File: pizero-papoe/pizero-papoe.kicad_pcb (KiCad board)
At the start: 2 copper layers, 81.8 x 30 mm, 67 parts, among them J1 RJ45-LED, P2 dnp-REF-182665-01, Q2 DMMT3906_Dual_PNP, Q3 Q_PMOS_GSD, T1 H2019FNL, U1 ENC28J60-I/ML, U2 TPS63070RNMR, U3 nostuff-AT24CS32-SSHM, U4 AP7365_SOT-23-5, Y1 25Mhz

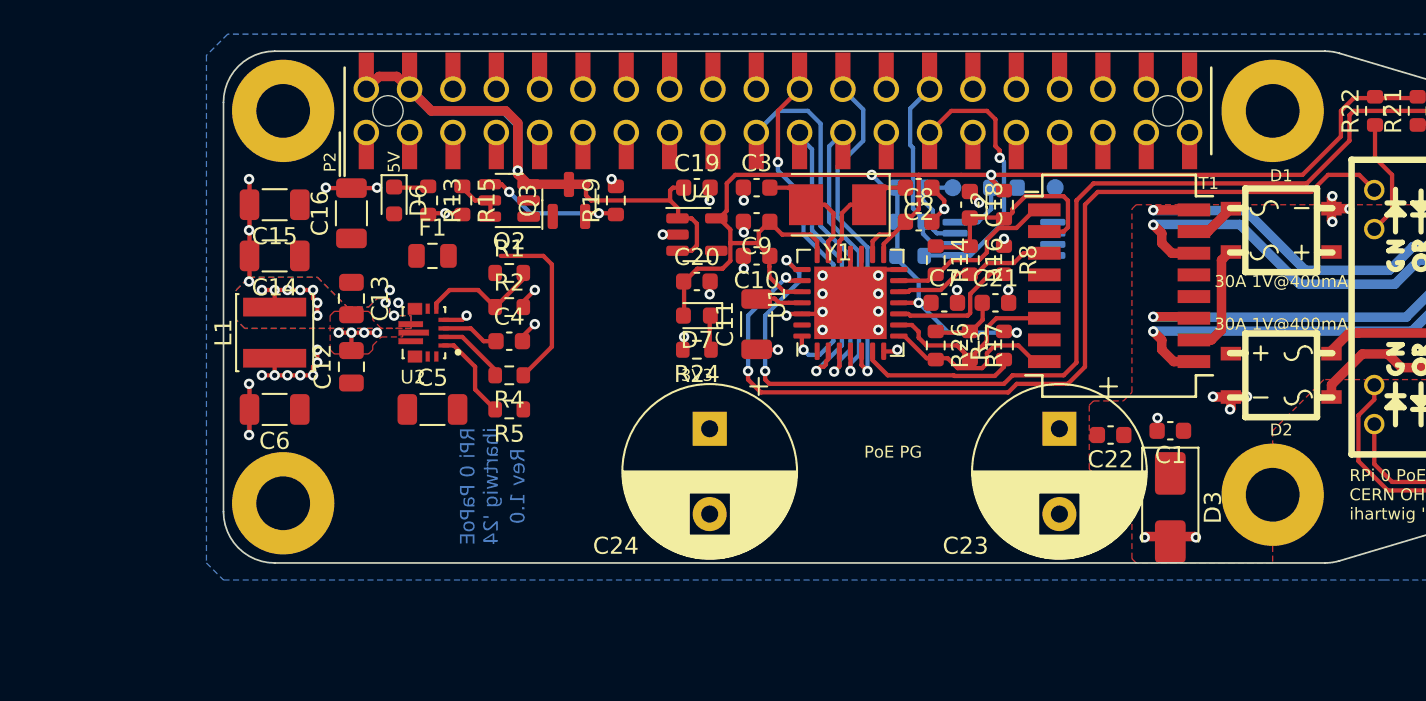
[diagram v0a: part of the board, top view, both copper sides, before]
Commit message: sch updates for RTL8153B and RJE7318800240
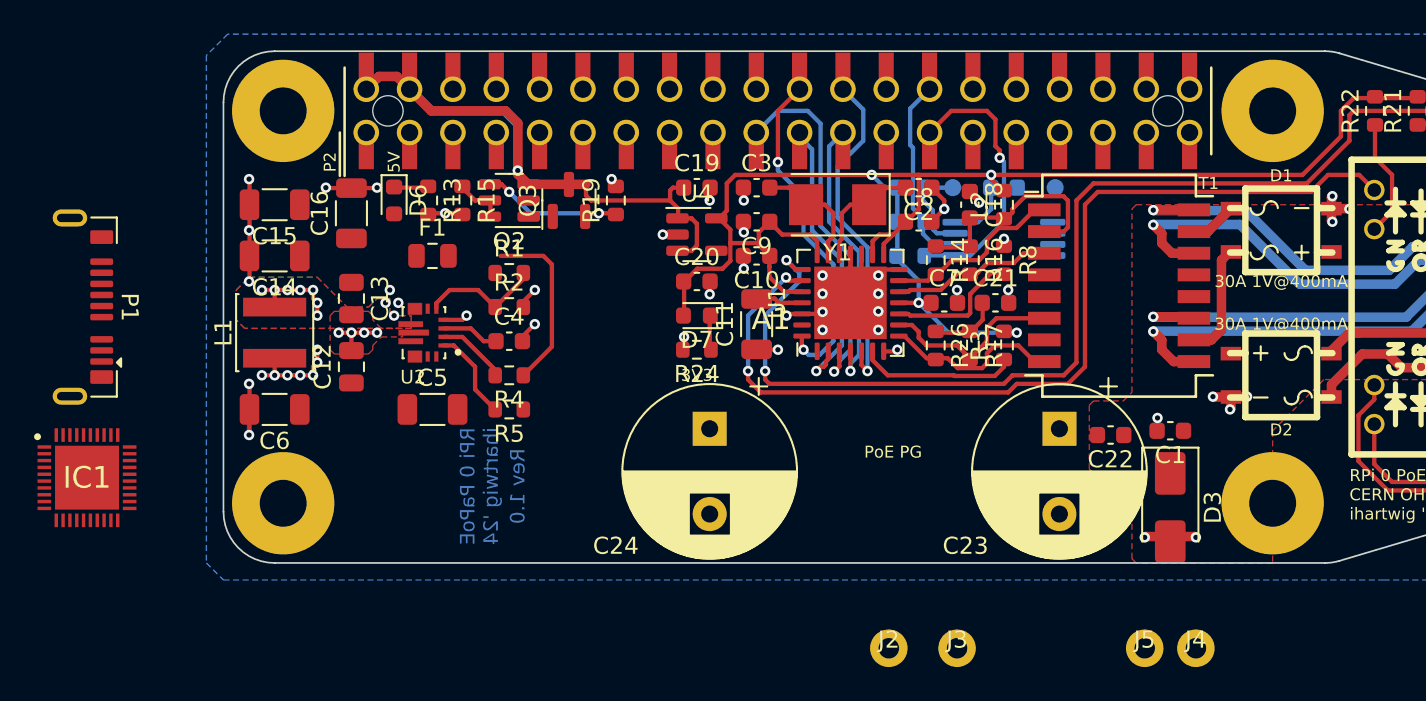
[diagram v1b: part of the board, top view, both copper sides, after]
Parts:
- removed H1, H2, H3, H4: hole-metalized-no4, pizero-poe-special:hole-m3
- added A1: Raspberry Pi Zero/W/2W, Raspberry_Pi_Zero_v.1.3_Hat:RPi_Zero_ZeroW_Zero2W_Hat_NoPads_NoHeader, F.Cu at (171.1, 107.7)
- added IC1: RTL8153B-VB-CG, pizero-poe-special:RTL8153B-VB-CG_QFN40P500X500X90-41N-D, F.Cu at (98.1, 102.7)
- added J2: PogoPin_01x01, pizero-poe-special:PogoPin_CPG-04-TH-TR, F.Cu at (145.1, 112.7)
- added J3: PogoPin_01x01, pizero-poe-special:PogoPin_CPG-04-TH-TR, F.Cu at (149.1, 112.7)
- added J4: PogoPin_01x01, pizero-poe-special:PogoPin_CPG-04-TH-TR, F.Cu at (163.1, 112.7)
- added J5: PogoPin_01x01, pizero-poe-special:PogoPin_CPG-04-TH-TR, F.Cu at (160.1, 112.7)
- added P1: USB_C_Plug_USB3.0_9P, pizero-poe-special:USB_C_Plug_G-Switch_GT-USB-8016A_9P_TopMnt_Horizontal, F.Cu at (97.1, 92.7)

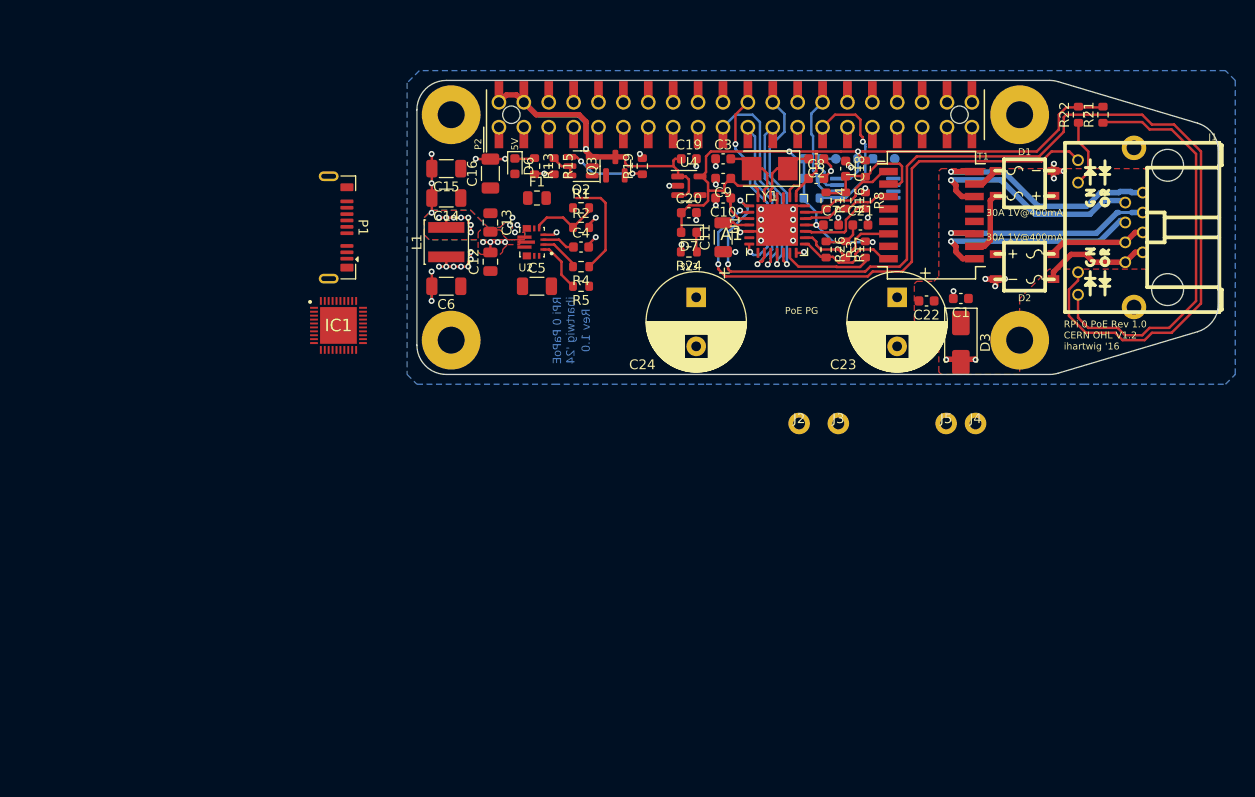
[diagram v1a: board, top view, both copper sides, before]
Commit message: complete RTL8153B sch
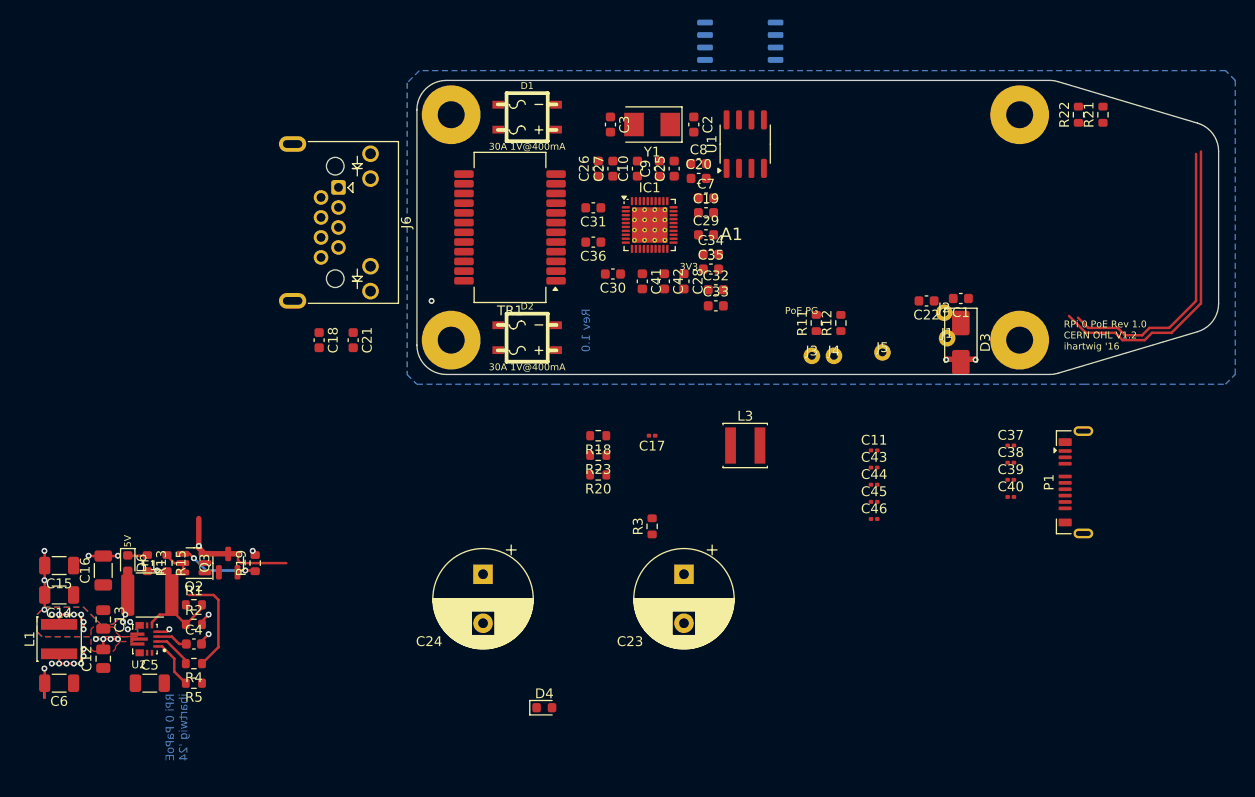
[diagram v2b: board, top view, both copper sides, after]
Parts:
- removed D7: LED Green, LED_SMD:LED_0603_1608Metric
- removed L2: BEAD, Resistor_SMD:R_0603_1608Metric
- removed P2: dnp-REF-182665-01, pizero-poe-special:Pin_Header_Straight_TH-SMT-NoPaste_2x20
- removed R14, R16, R17, R26: 49.9, Resistor_SMD:R_0603_1608Metric
- removed R24: 220, Resistor_SMD:R_0603_1608Metric
- removed R8: 2.32k, Resistor_SMD:R_0603_1608Metric
- removed T1: H2019FNL, pizero-poe-special:Transformer_Pulse_H2019FNL
- removed U4: AP7365_SOT-23-5, Package_TO_SOT_SMD:SOT-23-5
- removed W1, W2: TEST_1P, TestPoint:TestPoint_Pad_D1.0mm
- added C25: 0.1uf, Capacitor_SMD:C_0603_1608Metric, F.Cu at (132.3, 86.7)
- added C26: 0.1uf, Capacitor_SMD:C_0603_1608Metric, F.Cu at (124.6, 86.7)
- added C27: 0.1uf, Capacitor_SMD:C_0603_1608Metric, F.Cu at (126.1, 86.7)
- added C28: 0.1uf, Capacitor_SMD:C_0603_1608Metric, F.Cu at (133.3, 98.2)
- added C29: 0.1uf, Capacitor_SMD:C_0603_1608Metric, F.Cu at (135.6, 93.5)
- added C30: 0.1uf, Capacitor_SMD:C_0603_1608Metric, F.Cu at (126.1, 97.5)
- added C31: 0.1uf, Capacitor_SMD:C_0603_1608Metric, F.Cu at (124.1, 90.7)
- added C32: 4.7uF, Capacitor_SMD:C_0603_1608Metric, F.Cu at (136.6, 99.1)
- added C33: 0.1uf, Capacitor_SMD:C_0603_1608Metric, F.Cu at (136.6, 100.7)
- added C34: 1uF, Capacitor_SMD:C_0603_1608Metric, F.Cu at (136.1, 95.5)
- added C35: 0.1uf, Capacitor_SMD:C_0603_1608Metric, F.Cu at (136.1, 97.0)
- added C36: 0.1uf, Capacitor_SMD:C_0603_1608Metric, F.Cu at (124.1, 94.2)
- added C37: 0.1uF 0201, Capacitor_SMD:C_0201_0603Metric, F.Cu at (166.7, 115.0)
- added C38: 0.1uF 0201, Capacitor_SMD:C_0201_0603Metric, F.Cu at (166.7, 116.7)
- added C39: 0.1uF 0201, Capacitor_SMD:C_0201_0603Metric, F.Cu at (166.7, 118.5)
- added C40: 0.1uF 0201, Capacitor_SMD:C_0201_0603Metric, F.Cu at (166.7, 120.2)
- added C41: 0.1uf, Capacitor_SMD:C_0603_1608Metric, F.Cu at (129.1, 98.2)
- added C42: 0.1uf, Capacitor_SMD:C_0603_1608Metric, F.Cu at (131.3, 98.2)
- added C43: 0.1uF, Capacitor_SMD:C_0201_0603Metric, F.Cu at (152.8, 117.2)
- added C44: 0.1uF, Capacitor_SMD:C_0201_0603Metric, F.Cu at (152.8, 119.0)
- added C45: 0.1uF, Capacitor_SMD:C_0201_0603Metric, F.Cu at (152.8, 120.7)
- added C46: 0.1uF, Capacitor_SMD:C_0201_0603Metric, F.Cu at (152.8, 122.5)
- added D4: LED Orange, LED_SMD:LED_0603_1608Metric, F.Cu at (119.1, 141.7)
- added J6: RJ45_LED_AK_Shielded, pizero-poe-special:RJ45_Amphenol_RJE7318800xxx0x, F.Cu at (97.8, 92.2)
- added L3: 2.2uH, Inductor_SMD:L_Sunlord_SWPA4030S, F.Cu at (139.6, 115.0)
- added R11: 22, Resistor_SMD:R_0603_1608Metric, F.Cu at (146.8, 102.5)
- added R12: 22, Resistor_SMD:R_0603_1608Metric, F.Cu at (149.4, 102.5)
- added TR1: 30F-51NL, Transformer_SMD:Transformer_Ethernet_YDS_30F-51NL_SO-24_7.1x15.1mm, F.Cu at (115.6, 92.7)
- C11: value 10uf -> 0.1uF; footprint Capacitor_SMD:C_1206_3216Metric -> Capacitor_SMD:C_0201_0603Metric
- C17: value nostuff-0.1u -> 0.1uF; footprint Capacitor_SMD:C_0603_1608Metric -> Capacitor_SMD:C_0201_0603Metric; moved to F.Cu
- C18, C21: value 0.1uf -> 1nF
- C19, C20: value 1uF -> 4.7uF
- C2, C3: value 16pf -> 30pf
- F1: footprint Fuse:Fuse_0805_2012Metric -> pizero-poe-special:Fuse_2016_5041Metric
- IC1: footprint pizero-poe-special:RTL8153B-VB-CG_QFN40P500X500X90-41N-D -> Package_DFN_QFN:QFN-40-1EP_5x5mm_P0.4mm_EP3.6x3.6mm_ThermalVias
- J1: value RJ45-LED -> PogoPin_01x01; footprint pizero-poe-special:rj45-tyco-2-406549-7 -> pizero-poe-special:PogoPin_CPG-01-TH-TR
- J2, J3, J4, J5: footprint pizero-poe-special:PogoPin_CPG-04-TH-TR -> pizero-poe-special:PogoPin_CPG-01-TH-TR
- R18: value nostuff-1k -> 22-dnp; moved to F.Cu
- R20: value nostuff-3.9k -> 22-dnp; moved to F.Cu
- R21, R22: value 549 -> 1k
- R23: value nostuff-3.9k -> 10k; moved to F.Cu
- U1: value ENC28J60-I/ML -> 93LC46B; footprint Package_DFN_QFN:QFN-28-1EP_6x6mm_P0.65mm_EP4.25x4.25mm -> Package_SO:SOIC-8_3.9x4.9mm_P1.27mm
- U3: value nostuff-AT24CS32-SSHM -> MX25L3233FM1; footprint Package_SO:TSSOP-8_4.4x3mm_P0.65mm -> Package_SO:SOP-8_5.28x5.23mm_P1.27mm
- moved P1 81.3 mm to (174.1, 118.7), turned to 90 degrees
- moved C15 56.6 mm to (69.6, 127.2)
- moved C16 56.6 mm to (74.1, 127.7)
- moved D6 56.6 mm to (76.6, 127.0)
- moved Q2 56.6 mm to (83.3, 127.0)
- moved Q3 56.6 mm to (86.8, 127.0)
- moved R13 56.6 mm to (78.6, 127.0)
- moved R15 56.6 mm to (80.6, 127.0)
- moved R19 56.6 mm to (89.6, 127.0)
- moved C12 56.6 mm to (74.1, 136.7)
- moved C13 56.6 mm to (74.1, 132.7)
- moved C14 56.6 mm to (69.6, 130.2)
- moved C4 56.6 mm to (83.3, 135.2)
- moved C5 56.6 mm to (78.8, 139.2)
- moved C6 56.6 mm to (69.6, 139.2)
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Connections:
- C10 pad 1: +3V3 -> +1V0
- C11 pad 2: Net-(U1-VCAP) -> /TR1_CT
- C17 pad 1: +3V3 -> GND
- C17 pad 2: GND -> /TR1_CT
- C18 pad 1: GND -> /J1_SH_C
- C18 pad 2: Net-(T1-TDCT) -> GND
- C2 pad 2: /PHY_OSC1 -> /IC1_CKXTAL1
- C20 pad 1: +3V3 -> +1V0
- C21 pad 1: Net-(C21-Pad1) -> /J1_SH_C
- C3 pad 2: /PHY_OSC2 -> /IC1_CKXTAL2
- C7 pad 1: +3V3 -> /RPI_VBUS
- C8 pad 1: +3V3 -> +1V0
- C9 pad 1: +3V3 -> +1V0
- D1 pad 2: /DATA_PAIR_2 -> /J6_DB_C
- D1 pad 3: /DATA_PAIR_1 -> /J6_DA_C
- D2 pad 2: /SPARE_PAIR_2 -> /J6_DC_C
- D2 pad 3: /SPARE_PAIR_1 -> /J6_DD_C
- IC1 pad 1: unconnected-(IC1-MDIP0-Pad1) -> /IC1_MDIP0
- IC1 pad 10: unconnected-(IC1-MDIN3-Pad10) -> /IC1_MDIN3
- IC1 pad 11: unconnected-(IC1-AVDD33_1-Pad11) -> +3V3
- IC1 pad 12: unconnected-(IC1-U3SSTXN-Pad12) -> /IC1_U3SSTX_N
- IC1 pad 13: unconnected-(IC1-U3SSTXP-Pad13) -> /IC1_U3SSTX_P
- IC1 pad 14: unconnected-(IC1-U3VDD10-Pad14) -> +1V0
- IC1 pad 15: unconnected-(IC1-U3SSRXN-Pad15) -> /IC1_U3SSRX_N
- IC1 pad 16: unconnected-(IC1-U3SSRXP-Pad16) -> /IC1_U3SSRX_P
- IC1 pad 17: unconnected-(IC1-U2DM-Pad17) -> /IC1_U2DM
- IC1 pad 18: unconnected-(IC1-U2DP-Pad18) -> /IC1_U2DP
- IC1 pad 19: unconnected-(IC1-U2VDD10-Pad19) -> +1V0
- IC1 pad 2: unconnected-(IC1-MDIN0-Pad2) -> /IC1_MDIN0
- IC1 pad 20: unconnected-(IC1-AVDD33_2-Pad20) -> +3V3
- IC1 pad 21: unconnected-(IC1-VDD5-Pad21) -> /RPI_VBUS
- IC1 pad 22: unconnected-(IC1-DVDD10_UPS-Pad22) -> /IC1_DVDD10_UPS
- IC1 pad 23: unconnected-(IC1-DVDD33_1-Pad23) -> +3V3
- IC1 pad 24: unconnected-(IC1-EEDO/LED2/SPISDO/LANW/AKEB/GPIO-Pad24) -> /IC1_EED0_LED2
- IC1 pad 25: unconnected-(IC1-EEDI/SPISDI/ENSWREG-Pad25) -> /IC1_EEDI_ENSWREG
- IC1 pad 26: unconnected-(IC1-VDDREG33-Pad26) -> /RPI_VBUS
- IC1 pad 27: unconnected-(IC1-VDDREG5-Pad27) -> /RPI_VBUS
- IC1 pad 28: unconnected-(IC1-REGOUT-Pad28) -> /IC1_REGOUT
- IC1 pad 29: unconnected-(IC1-GND-Pad29) -> GND
- IC1 pad 3: unconnected-(IC1-AVDD10_1-Pad3) -> +1V0
- IC1 pad 30: unconnected-(IC1-EESK/LED1/SPISCK-Pad30) -> /IC1_LED1_SPISCK
- IC1 pad 31: unconnected-(IC1-EECS-Pad31) -> /IC1_EECS
- IC1 pad 32: unconnected-(IC1-LED0/SPICSB-Pad32) -> /IC1_LED0_SPICSB
- IC1 pad 33: unconnected-(IC1-DVDD33_2-Pad33) -> +3V3
- IC1 pad 34: unconnected-(IC1-DVDD10-Pad34) -> +1V0
- IC1 pad 35: unconnected-(IC1-CKXTAL1-Pad35) -> /IC1_CKXTAL1
- IC1 pad 36: unconnected-(IC1-CKXTAL2-Pad36) -> /IC1_CKXTAL2
- IC1 pad 37: unconnected-(IC1-AVDD10_3-Pad37) -> +1V0
- IC1 pad 39: unconnected-(IC1-AVDD33_3-Pad39) -> +3V3
- IC1 pad 4: unconnected-(IC1-MDIP1-Pad4) -> /IC1_MDIP1
- IC1 pad 40: unconnected-(IC1-AVDD33_4-Pad40) -> +3V3
- IC1 pad 41: unconnected-(IC1-EP-Pad41) -> GND
- IC1 pad 5: unconnected-(IC1-MDIN1-Pad5) -> /IC1_MDIN1
- IC1 pad 6: unconnected-(IC1-MDIP2-Pad6) -> /IC1_MDIP2
- IC1 pad 7: unconnected-(IC1-MDIN2-Pad7) -> /IC1_MDIN2
- IC1 pad 8: unconnected-(IC1-AVDD10_2-Pad8) -> +1V0
- IC1 pad 9: unconnected-(IC1-MDIP3-Pad9) -> /IC1_MDIP3
- J1 pad 1: /TPOUT_T+ -> GND
- J2 pad 1: unconnected-(J2-Pin_1-Pad1) -> /RPI_VBUS
- J3 pad 1: unconnected-(J3-Pin_1-Pad1) -> /J4_U2DM
- J4 pad 1: unconnected-(J4-Pin_1-Pad1) -> /J5_U2DP
- J5 pad 1: unconnected-(J5-Pin_1-Pad1) -> GND
- P1 pad A2: unconnected-(P1-TX1+-PadA2) -> /IC1_U3SSTX_C_P
- P1 pad A3: unconnected-(P1-TX1--PadA3) -> /IC1_U3SSTX_C_N
- P1 pad A6: unconnected-(P1-D+-PadA6) -> /P1_U2DP
- P1 pad A7: unconnected-(P1-D--PadA7) -> /P1_U2DM
- P1 pad B10: unconnected-(P1-RX1--PadB10) -> /IC1_U3SSRX_C_N
- P1 pad B11: unconnected-(P1-RX1+-PadB11) -> /IC1_U3SSRX_C_P
- R18 pad 1: +3V3 -> /P1_U2DM
- R18 pad 2: Net-(U3-WP) -> /IC1_U2DM
- R20 pad 1: +3V3 -> /P1_U2DP
- R20 pad 2: /GPIO0_ID_SD -> /IC1_U2DP
- R21 pad 1: /LEDB_A -> /J1_LED_YL_A
- R21 pad 2: +3V3 -> GND
- R22 pad 1: /LEDA_A -> /J1_LED_GN_A
- R22 pad 2: +3V3 -> GND
- R23 pad 2: /GPIO1_ID_SC -> /IC1_EEDI_ENSWREG
- R3 pad 1: Net-(U1-~{RESET}) -> Net-(D4-K)
- R3 pad 2: +3V3 -> GND
- U1 pad 1: unconnected-(U1-~{WOL}-Pad1) -> /IC1_EECS
- U1 pad 2: /GPIO9_MISO -> /IC1_LED1_SPISCK
- U1 pad 3: /GPIO10_MOSI -> /IC1_EEDI_ENSWREG
- U1 pad 4: /GPIO11_SCLK -> /IC1_EED0_LED2
- U1 pad 5: /GPIO8_CE0# -> GND
- U1 pad 6: Net-(U1-~{RESET}) -> unconnected-(U1-NC-Pad6)
- U1 pad 7: GND -> unconnected-(U1-NC-Pad7)
- U1 pad 8: /TPIN- -> +3V3
- U3 pad 1: GND -> /IC1_LED0_SPICSB
- U3 pad 2: GND -> /IC1_EED0_LED2
- U3 pad 3: GND -> +3V3
- U3 pad 5: /GPIO0_ID_SD -> /IC1_EEDI_ENSWREG
- U3 pad 6: /GPIO1_ID_SC -> /IC1_LED1_SPISCK
- U3 pad 7: Net-(U3-WP) -> +3V3
- Y1 pad 1: /PHY_OSC1 -> /IC1_CKXTAL1
- Y1 pad 2: /PHY_OSC2 -> /IC1_CKXTAL2
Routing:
- net /LEDB_K: track 108.6 -> 0.00 mm, vias 2 -> 0
- net +3V3: track 97.2 -> 0.00 mm, vias 4 -> 0
- net /LEDA_K: track 56.1 -> 0.00 mm, vias 2 -> 0
- net GND: track 77.9 -> 26.0 mm, vias 47 -> 18
- net /LEDB_A: track 42.4 -> 0.00 mm
- net (no net): track 91.1 -> 53.4 mm
- net /J1_LED_YL_A: track 0.00 -> 29.2 mm
- net /TPOUT_T+: track 24.1 -> 0.00 mm, vias 1 -> 0
- net /TPOUT_T-: track 23.3 -> 0.00 mm, vias 1 -> 0
- net /GPIO10_MOSI: track 22.9 -> 0.00 mm, vias 1 -> 0
- net /TPIN_T+: track 22.9 -> 0.00 mm, vias 1 -> 0
- net /TPIN_T-: track 22.2 -> 0.00 mm, vias 1 -> 0
- net /GPIO25: track 21.0 -> 0.00 mm, vias 2 -> 0
- net /GPIO8_CE0#: track 21.0 -> 0.00 mm, vias 1 -> 0
- net /GPIO9_MISO: track 18.5 -> 0.00 mm, vias 1 -> 0
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- removed copper zone on F.Cu, net /POE_VP

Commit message: pcb routing for RTL8153B and RJE7318800240
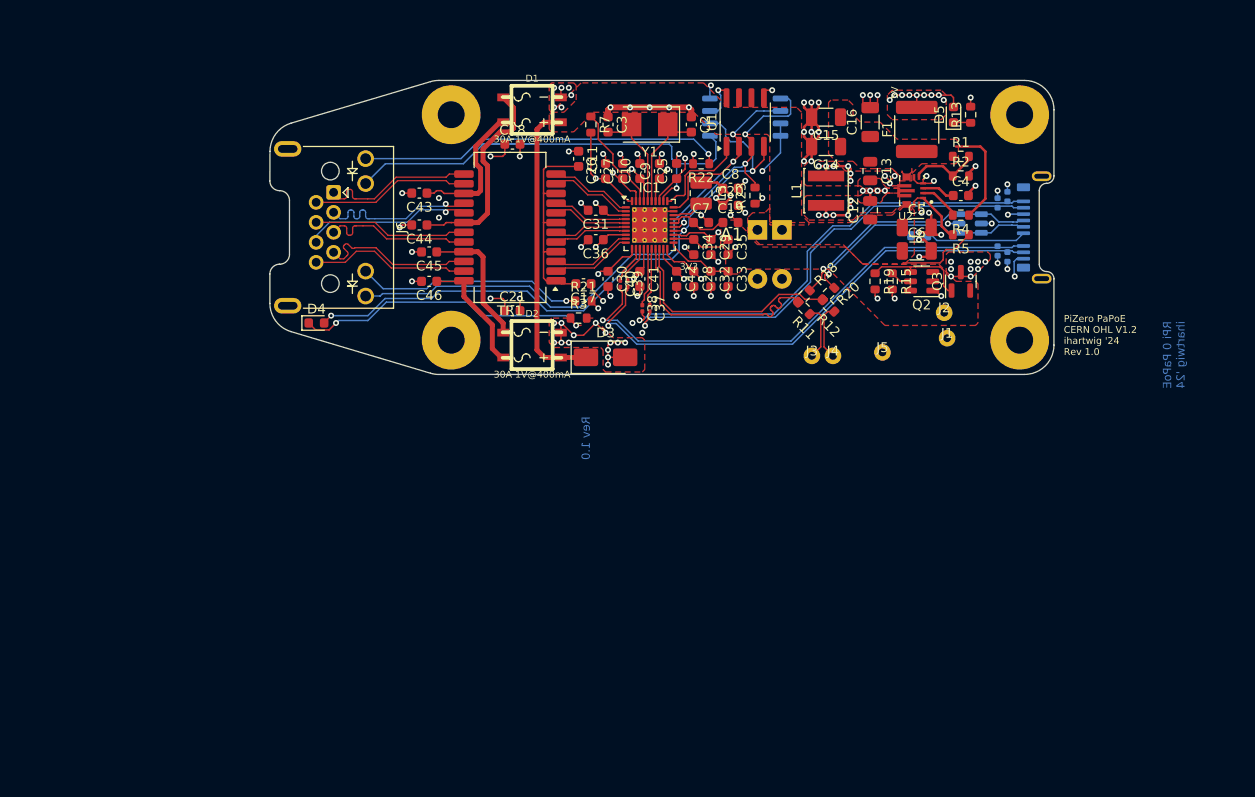
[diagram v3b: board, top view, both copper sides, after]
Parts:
- removed C1, C22: 0.1uf 100V, Capacitor_SMD:C_0603_1608Metric
- added D5: LED Green, LED_SMD:LED_0603_1608Metric, F.Cu at (160.8, 81.2)
- added D7: TPD1E01B04-dnp, Diode_SMD:D_0402_1005Metric, B.Cu at (165.3, 95.1)
- added D8: TPD1E01B04-dnp, Diode_SMD:D_0402_1005Metric, B.Cu at (165.3, 90.2)
- added D9: TPD1E01B04-dnp, Diode_SMD:D_0402_1005Metric, B.Cu at (166.3, 89.5)
- added R6: 5.1k, Resistor_SMD:R_0603_1608Metric, B.Cu at (157.3, 93.5)
- added R7: 10k, Resistor_SMD:R_0603_1608Metric, F.Cu at (123.8, 82.2)
- added U4: WE-TVS-82400102-dnp, Package_TO_SOT_SMD:SOT-23-6, B.Cu at (162.6, 92.3)
- C11, C17, C43, C44, C45, C46: footprint Capacitor_SMD:C_0201_0603Metric -> Capacitor_SMD:C_0603_1608Metric
- C23, C24, P1: moved to B.Cu
- D6: value LED Green -> TPD1E01B04-dnp; footprint LED_SMD:LED_0603_1608Metric -> Diode_SMD:D_0402_1005Metric; moved to B.Cu
- L3: footprint Inductor_SMD:L_Sunlord_SWPA4030S -> Inductor_SMD:L_1008_2520Metric
- moved C6 98.0 mm to (157.1, 95.1), turned to 0 degrees
- moved R13 95.7 mm to (162.6, 81.2), turned to 90 degrees
- moved D6 95.0 mm to (166.3, 95.7)
- moved F1 91.5 mm to (157.1, 82.7), turned to 90 degrees
- moved C5 91.0 mm to (157.1, 92.7)
- moved C12 90.6 mm to (152.3, 91.0)
- moved C13 90.6 mm to (152.3, 87.0)
- moved C14 90.6 mm to (147.8, 84.5)
- moved C15 90.6 mm to (147.8, 81.5)
- moved C16 90.6 mm to (152.3, 82.0)
- moved C4 90.6 mm to (161.6, 89.5)
- moved L1 90.6 mm to (147.8, 89.0)
- moved R1 90.6 mm to (161.6, 85.5)
- moved R2 90.6 mm to (161.6, 87.5)
- moved R4 90.6 mm to (161.6, 91.5)
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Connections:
- net /IC1_MDIN0 renamed /IC1_MDI0_N
- net /IC1_MDIN1 renamed /IC1_MDI1_N
- net /IC1_MDIN2 renamed /IC1_MDI2_N
- net /IC1_MDIN3 renamed /IC1_MDI3_N
- net /IC1_MDIP0 renamed /IC1_MDI0_P
- net /IC1_MDIP1 renamed /IC1_MDI1_P
- net /IC1_MDIP2 renamed /IC1_MDI2_P
- net /IC1_MDIP3 renamed /IC1_MDI3_P
- net /IC1_U2DM renamed /IC1_U2DN
- net /IC1_U3SSRX_C_N renamed /P1_U3SSRX_N
- net /IC1_U3SSRX_C_P renamed /P1_U3SSRX_P
- net /IC1_U3SSTX_C_N renamed /P1_U3SSTX_N
- net /J4_U2DM renamed /A1_U2DN
- net /J5_U2DP renamed /A1_U2DP
- net /J6_1_DA_P renamed /J6_DA_P
- net /J6_2_DA_N renamed /J6_DA_N
- net /J6_3_DB_P renamed /J6_DB_P
- net /J6_4_DC_P renamed /J6_DC_P
- net /J6_5_DC_N renamed /J6_DC_N
- net /J6_6_DB_N renamed /J6_DB_N
- net /J6_7_DD_P renamed /J6_DD_P
- net /J6_8_DD_N renamed /J6_DD_N
- net /P1_U2DM renamed /P1_U2DN
- C39 pad 2: /IC1_U3SSTX_C_P -> /P1_U3SSTX_P
- D6 pad 1: Net-(D6-K) -> /P1_U3SSTX_P
- D6 pad 2: +5V -> GND
- IC1 pad 38: unconnected-(IC1-RSET-Pad38) -> /IC1_RST
- P1 pad A1: Net-(P1-GND-PadA1) -> GND
- P1 pad A2: /IC1_U3SSTX_C_P -> /P1_U3SSTX_P
- P1 pad A5: unconnected-(P1-CC-PadA5) -> /P1_CC
- P1 pad A9: Net-(P1-VBUS-PadA4) -> +5V
- R13 pad 1: Net-(D6-K) -> Net-(D5-K)
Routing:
- net GND: track 26.0 -> 124.7 mm, vias 18 -> 89
- net /IC1_EED0_LED2: track 0.00 -> 65.3 mm, vias 0 -> 3
- net /IC1_LED1_SPISCK: track 0.00 -> 65.1 mm, vias 0 -> 2
- net /IC1_LED0_SPICSB: track 0.00 -> 57.6 mm, vias 0 -> 1
- net (no net): track 53.4 -> 0.00 mm, vias 3 -> 0
- net /P1_U3SSTX_N: track 0.00 -> 52.3 mm, vias 0 -> 1
- net /P1_U3SSTX_P: track 0.00 -> 52.1 mm, vias 0 -> 1
- net +3V3: track 0.00 -> 51.1 mm, vias 0 -> 9
- net /P1_U3SSRX_N: track 0.00 -> 47.3 mm, vias 0 -> 1
- net /P1_U3SSRX_P: track 0.00 -> 47.3 mm, vias 0 -> 1
- net /POE_VP: track 0.00 -> 41.2 mm
- net /J1_LED_GN_A: track 0.00 -> 37.5 mm, vias 0 -> 1
- net Net-(D4-K): track 0.00 -> 30.7 mm, vias 0 -> 2
- net +1V0: track 0.00 -> 29.5 mm, vias 0 -> 8
- net /J1_SH_C: track 0.00 -> 29.3 mm, vias 0 -> 8
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- added copper zone on In2.Cu, net +1V0
- added copper zone on In2.Cu, net +3V3
- added copper zone on F.Cu, net +5V
- added copper zone on In1.Cu, net +5V
- added copper zone on In1.Cu, net /J1_SH_C
- added copper zone on In2.Cu, net /J1_SH_C
- added copper zone on F.Cu, net /POE_VP
- added copper zone on F.Cu, net /RPI_VBUS
- added copper zone on F.Cu, net /U2_L1
- added copper zone on In1.Cu, net /U2_L1
- added copper zone on In1.Cu, net /U2_L2
- added copper zone on F.Cu, net /U2_VOUT
- added copper zone on In1.Cu, net GND
- added copper zone on In2.Cu, net GND
- removed copper zone on B.Cu, net /U2_L2
- removed copper zone on B.Cu, net GND
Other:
- board size 81.8 x 30 mm -> 80 x 30 mm
- copper layers 2 -> 4
- board text added: "PiZero PaPoE CERN OHL V1.2 ihartwig '24 Rev 1.0"
- board text removed: "PoE PG"
- board text removed: "RPi 0 PoE Rev 1.0 CERN OHL V1.2 ihartwig '16"
